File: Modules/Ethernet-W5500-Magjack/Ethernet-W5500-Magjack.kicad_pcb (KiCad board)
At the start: 4 copper layers, 42 x 55 mm, 37 parts, among them J2 ARJM11C7-114-BA-EW2, U3 W5500, Y1 25.000MHz CL=12pF

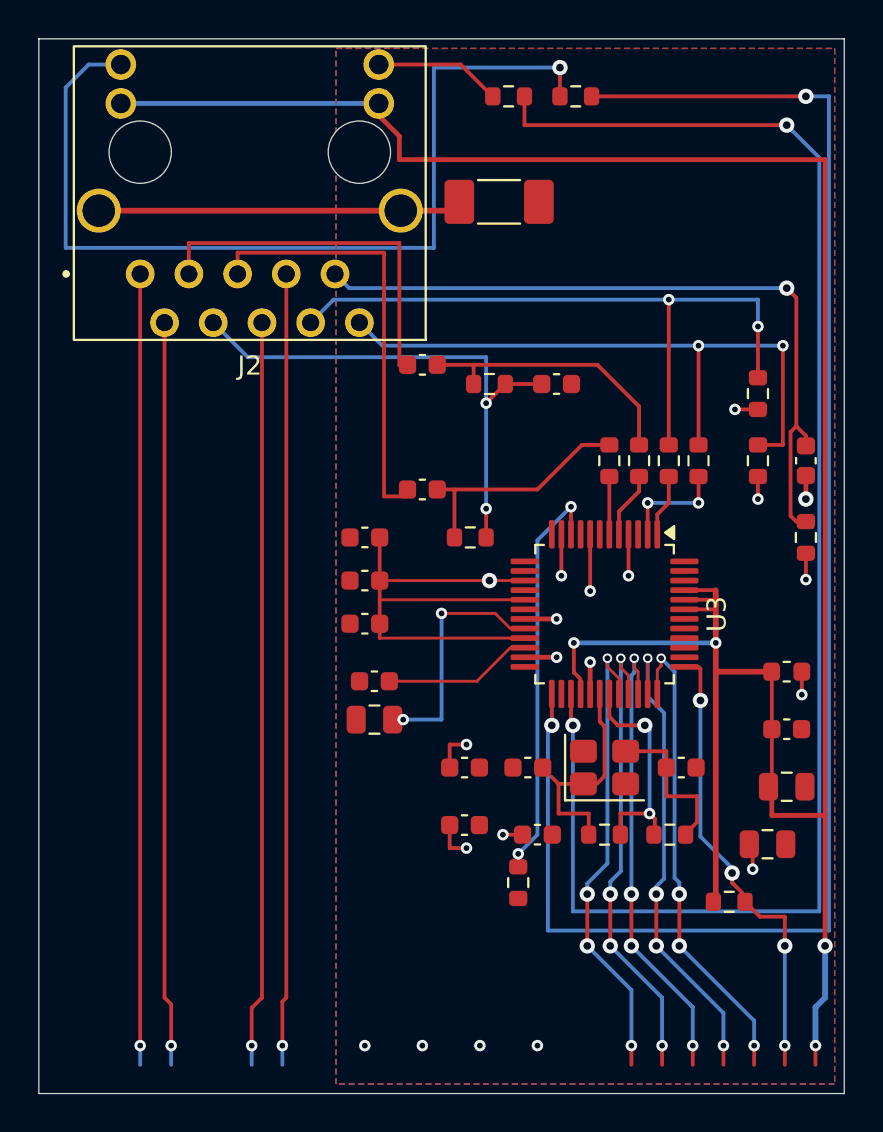
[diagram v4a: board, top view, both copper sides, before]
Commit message: Apply the review fixes to five boards and set solid power pads
Plans were proven on scratch copies, then applied with KiCad's own pcbnew
Python API, so KiCad writes every file. Each board: DRC 0 errors, 0
unconnected, 0 parity, and the canary fires.

Ethernet and PoE module (R1-1, R1-2, R1-3):
- The fanout rule no longer matches zones.
- Chip-side copper keeps 1.0 mm from the line-side jack pads (was 0.26 mm):
  MDI_RDP, MDI_RDN, RCT and LED_LINK_K rerouted. A 1.0 mm rule enforces it.
  The VC1P lane passes J2.8 at 0.42 mm inside the jack pad field, and only
  that pair is excepted.
- GND vias: Ethernet 8 to 42, PoE 11 to 55. No starved thermal remains.

Buck (R2-2, R2-5): three GND vias at U8.1, C100.2 and C101.2. TP3 sits
against R61.1, with a courtyard rule scoped to that pair.
USBC (R2-4): U2 moves 3 mm toward J1, with two GND vias at U2.2.
MCU (R1-9): C2 sits 1.71 mm from U1 pin 3 (was 23.5 mm), with a courtyard
rule scoped to C2 and U1.
Solid zone connections (R2-3) on U8, L30, C100 to C104, C108 to C111 and J1.

Co-Authored-By: Claude Opus 5.5 (1M context) <noreply@anthropic.com>
Claude-Session: https://claude.ai/code/session_01ErAAfkmF4h3T5yfrw21utF
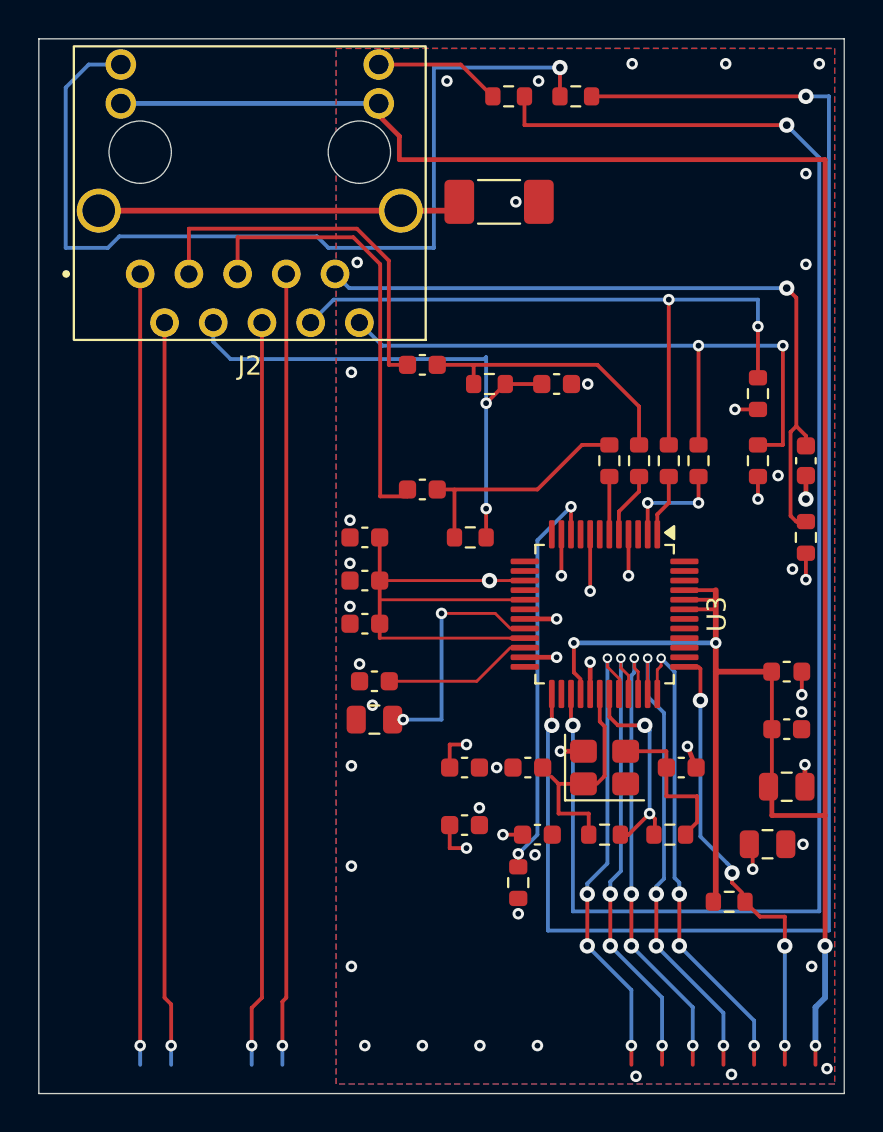
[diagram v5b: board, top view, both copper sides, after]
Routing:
- net GND: track 3.49 -> 7.03 mm, vias 8 -> 42
- net /MDI_RDP: track 23.0 -> 23.8 mm
- net /RCT: track 27.2 -> 27.9 mm
- net /XO: track 11.4 -> 10.8 mm
- net /MDI_RDN: track 19.4 -> 19.9 mm
